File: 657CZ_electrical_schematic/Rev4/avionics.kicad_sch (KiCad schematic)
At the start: 14 parts, among them SW11 G3X

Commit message: added Locations for outstanding components
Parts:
- FH6: LocLoad (0,0,0)R40 -> (35,20,-4)R40
- LRU10-C: LocLoad (0,0,0)L6.0 -> (30.3,19.7,.4)L6.0
- LRU10-N: LocLoad (0,0,0)L0.6 -> (32.4,16.2,.9)L0.6
- LRU11: LocLoad (0,0,0)L0.2 -> (37.7,22.,1.9)L0.2
- LRU21: LocLoad (0,0,0)L7.5 -> (30.2,18.9,-17.4)L7.5
- LRU22: LocLoad (0,0,0)L2.31 -> (30.25,19.7,.35)L2.31
- LRU24: LocLoad (0,0,0)L0.2 -> (35.3,1.3,12.2)L0.2
- LRU25: LocLoad (0,0,0)L0.1 -> (166,16,-62)L0.1
- LRU26: LocLoad (0,0,0)L0.25 -> (37.5,21.,-6.)L0.25
- LRU27: LocLoad (0,0,0)L0.2 -> (24.3,3.4,5.)L0.2
- LRU28: LocLoad (0,0,0)L1.3 -> (32,20,-5)L1.3
- LRU32: LocLoad (0,0,0)L0.43 -> (121.8,29.8,10.)L0.43
- LRU33: LocLoad (0,0,0)L2.0 -> (38.5,18.9,6.)L2.0
- SW11: LocLoad (0,0,0)R20 -> (41.3,21.6,-17.9)R20
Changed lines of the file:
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@@
 			)
 		)
-		(property "LocLoad" "(0,0,0)L2.31"
+		(property "LocLoad" "(30.25,19.7,.35)L2.31"
 			(at 45.72 62.23 0)
 			(effects
@@
 			)
 		)
-		(property "LocLoad" "(0,0,0)L0.43"
+		(property "LocLoad" "(121.8,29.8,10.)L0.43"
 			(at 119.38 96.52 0)
 			(effects
@@
 			)
 		)
-		(property "LocLoad" "(0,0,0)L0.6"
+		(property "LocLoad" "(32.4,16.2,.9)L0.6"
 			(at 45.72 86.36 0)
 			(effects
@@
 			)
 		)
-		(property "LocLoad" "(0,0,0)L2.0"
+		(property "LocLoad" "(38.5,18.9,6.)L2.0"
 			(at 113.03 106.68 0)
 			(effects
@@
 			)
 		)
-		(property "LocLoad" "(0,0,0)L0.2"
+		(property "LocLoad" "(24.3,3.4,5.)L0.2"
 			(at 125.73 86.36 0)
 			(effects
@@
 			)
 		)
-		(property "LocLoad" "(0,0,0)L1.3"
+		(property "LocLoad" "(32,20,-5)L1.3"
 			(at 45.72 27.94 0)
 			(effects
@@
 			)
 		)
-		(property "LocLoad" "(0,0,0)L0.25"
+		(property "LocLoad" "(37.5,21.,-6.)L0.25"
 			(at 45.72 50.8 0)
 			(effects
@@
 			)
 		)
-		(property "LocLoad" "(0,0,0)L0.1"
+		(property "LocLoad" "(166,16,-62)L0.1"
 			(at 45.72 39.37 0)
 			(effects
@@
 			)
 		)
-		(property "LocLoad" "(0,0,0)R40"
+		(property "LocLoad" "(35,20,-4)R40"
 			(at 105.41 64.77 90)
 			(effects
@@
 			)
 		)
-		(property "LocLoad" "(0,0,0)L6.0"
+		(property "LocLoad" "(30.3,19.7,.4)L6.0"
 			(at 238.76 43.18 0)
 			(effects
@@
 			)
 		)
-		(property "LocLoad" "(0,0,0)L0.2"
+		(property "LocLoad" "(35.3,1.3,12.2)L0.2"
 			(at 132.08 76.2 0)
 			(effects
@@
 			)
 		)
-		(property "LocLoad" "(0,0,0)L0.2"
+		(property "LocLoad" "(37.7,22.,1.9)L0.2"
 			(at 237.49 31.75 0)
 			(effects
@@
 			)
 		)
-		(property "LocLoad" "(0,0,0)L7.5"
+		(property "LocLoad" "(30.2,18.9,-17.4)L7.5"
 			(at 45.72 73.66 0)
 			(effects
@@
 			)
 		)
-		(property "LocLoad" "(0,0,0)R20"
+		(property "LocLoad" "(41.3,21.6,-17.9)R20"
 			(at 99.06 53.34 0)
 			(effects

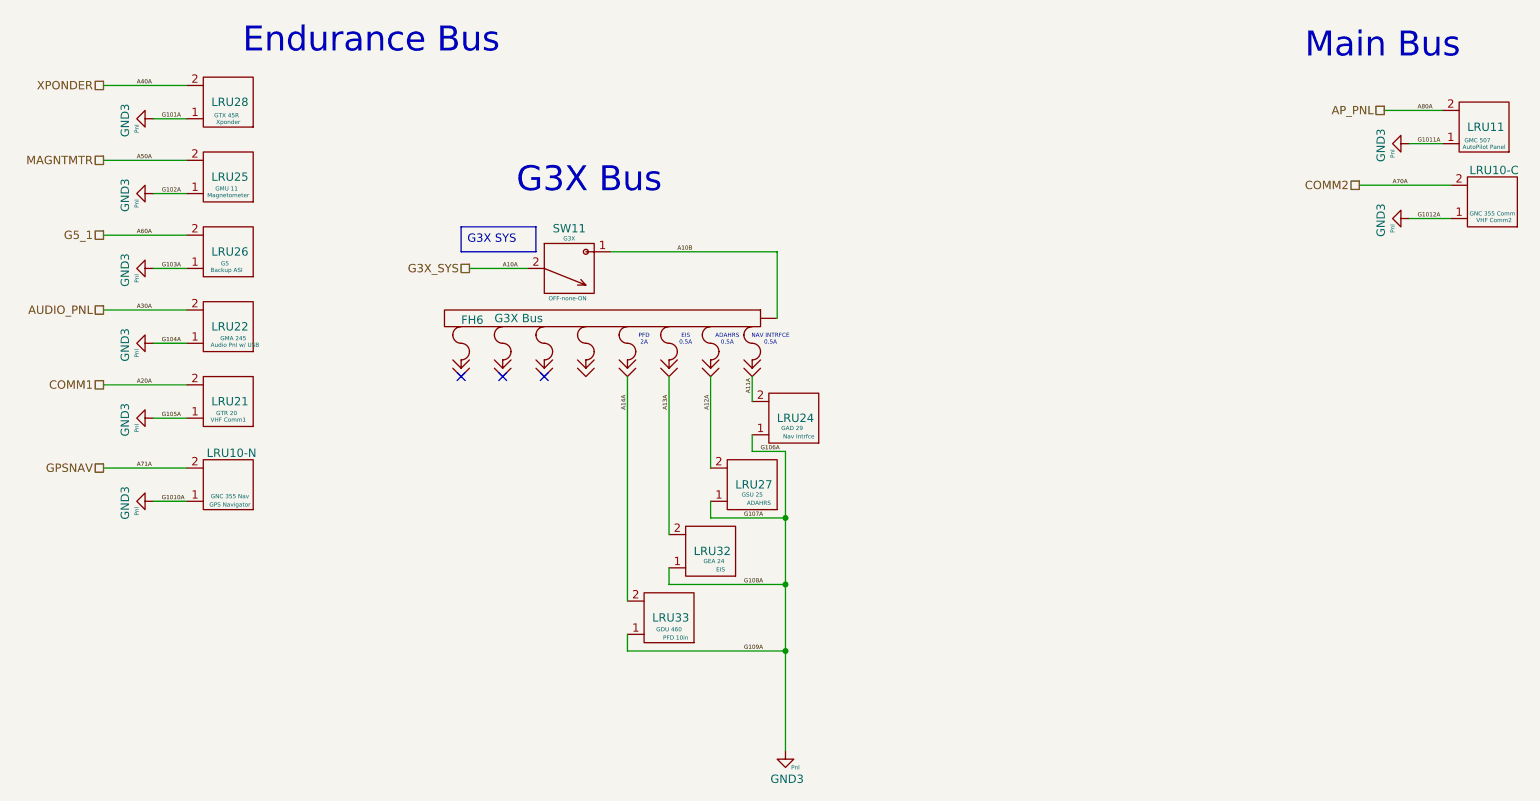
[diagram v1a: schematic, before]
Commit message: corrected comm1,2 to main/ebus, connected lightspeed to ebus
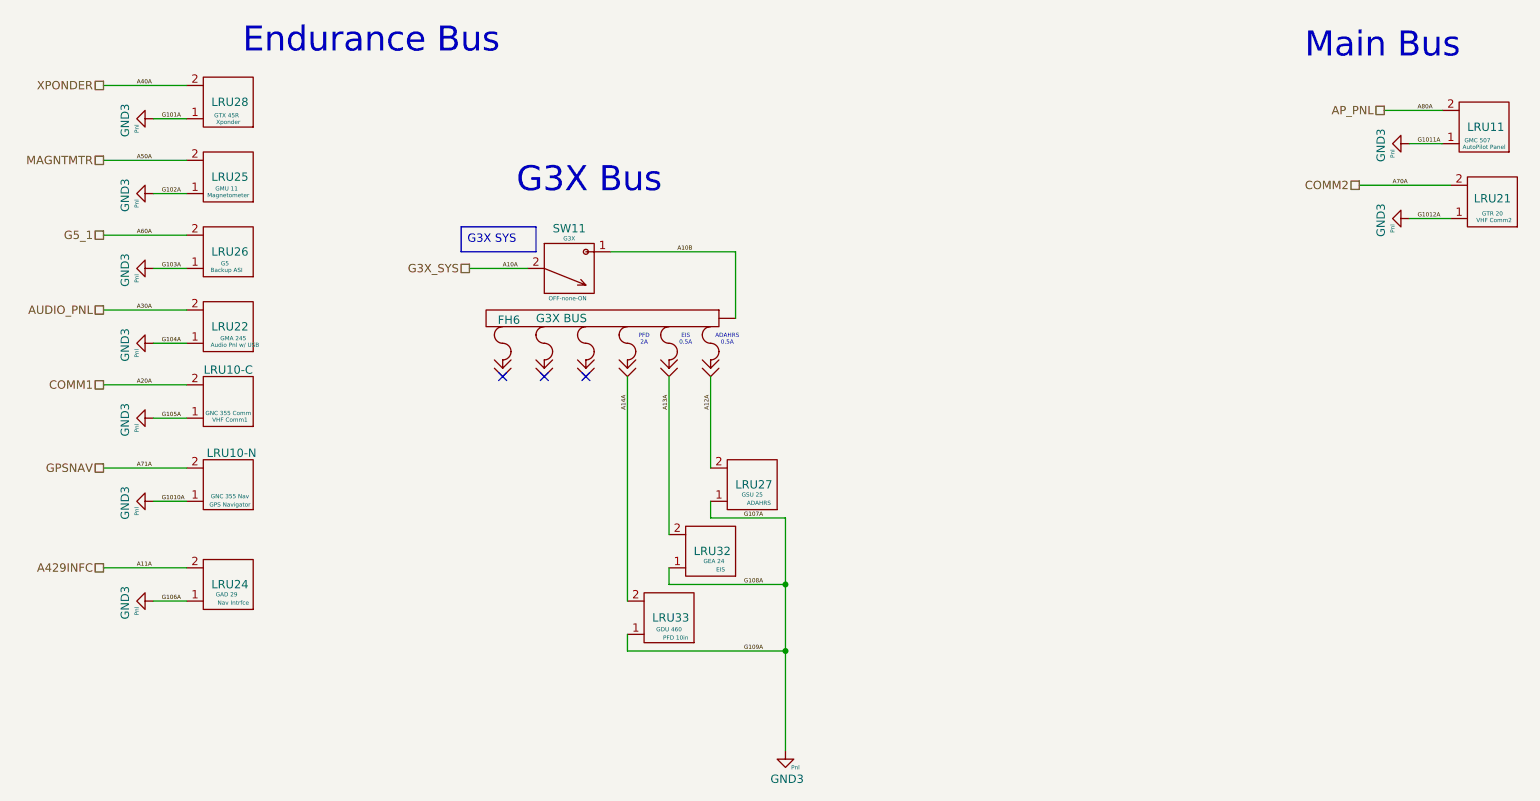
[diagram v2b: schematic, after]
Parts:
- removed FH6: G3X Bus, symbol AeroElectricConnectionSymbols:Fuse_Holder_8x
- added FH6: G3X BUS, symbol AeroElectricConnectionSymbols:Fuse_Holder_6x
- LRU10-C: renamed from LRU21; value val A -> ~
- renumbered LRU10-C to LRU21
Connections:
- net A10B: now also FH6.1 (Pwr)
- net A12A: now also FH6.Val_A (Desc)
- net A13A: now also FH6.Val_A (Desc)
- net A14A: now also FH6.Val_A (Desc)
- net A11A renamed A429INFC
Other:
- note removed: "NAV INTRFCE 0.5A"
- moved on the sheet: LRU24

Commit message: added LocLoad to FH6 G3X fuse block
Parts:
- FH6: LocLoad (none) -> (39.6,4.8,-1)R60
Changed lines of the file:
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@@
+			)
+		)
+		(property "LocLoad" "(39.6,4.8,-1)R60"
+			(at 102.87 64.77 90)
+			(effects
+				(font
+					(size 1.27 1.27)
+				)
+				(hide yes)
 			)
 		)
